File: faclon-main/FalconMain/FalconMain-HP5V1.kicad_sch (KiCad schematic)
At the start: 0 parts

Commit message: Reorganize
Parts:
- added C40, C53: 100uF, Capacitor_THT:CP_Radial_D8.0mm_P3.50mm, symbol Device:C_Polarized_Small
- added C41, C42, C43, C44: 10uF, Capacitor_SMD:C_1210_3225Metric, symbol Device:C_Small
- added C45, C47: 100nF, Capacitor_SMD:C_0402_1005Metric, symbol Device:C_Small
- added C46: 1uF, Capacitor_SMD:C_0603_1608Metric, symbol Device:C_Small
- added C48: 510pF, Capacitor_SMD:C_0402_1005Metric, symbol Device:C_Small
- added C49, C50, C51, C52: 47uF, Capacitor_SMD:C_1210_3225Metric, symbol Device:C_Small
- added C54: 51pF, Capacitor_SMD:C_0402_1005Metric, symbol Device:C_Small
- added C55: 1.5nF, Capacitor_SMD:C_0402_1005Metric, symbol Device:C_Small
- added L5: 2.0uH, JetkovKiCADLib:WE-HCI_1365_7443551, symbol Device:L_Small
- added Q22, Q23: Q_NMOS_LFPAK, JetkovKiCADLib:LFPACK56-S08_SOT669_NXP, symbol JetkovKiCADLib:Q_NMOS_LFPAK
- added R58, R59: 0R, Resistor_SMD:R_0402_1005Metric, symbol Device:R_Small
- added R60: DNP, Resistor_SMD:R_0402_1005Metric, symbol Device:R_Small
- added R61: 49.9k, Resistor_SMD:R_0402_1005Metric, symbol Device:R_Small
- added R62: 2R, Resistor_SMD:R_0402_1005Metric, symbol Device:R_Small
- added R63, R64: 80.6k, Resistor_SMD:R_0402_1005Metric, symbol Device:R_Small
- added R65: 27.4k, Resistor_SMD:R_0402_1005Metric, symbol Device:R_Small
- added R66: 100k, Resistor_SMD:R_0402_1005Metric, symbol Device:R_Small
- added R67: 15k, Resistor_SMD:R_0402_1005Metric, symbol Device:R_Small
- added U7: ADP1883ARMZ-0.6-R7, JetkovKiCADLib:10-MSOP_RM-10_AD, symbol JetkovKiCADLib:ADP1883ARMZ-0.6-R7
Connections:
- new net: R63.1, R67.2, U7.3 (FB)
- new net: C47.1, U7.10 (BST)
- new net: C48.1, C54.2, U7.2 (COMP/EN)
- new net: C45.2, C46.1, R59.1, U7.5 (VDD)
- new net: Q23.4 (G), R66.2, U7.6 (DRVL)
- new net: R58.2, U7.8 (DRVH)
- new net: C47.2, L5.1, Q22.1 (S), Q22.2 (S), Q22.3 (S), Q23.5 (D), R62.2, U7.9 (SW)
- new net: C48.2, R65.2
- new net: Q22.4 (G), R58.1
- new net: C55.1, R62.1
- new net +4V_SW: R59.2
- new net +5V1: C49.1, C50.1, C51.1, C52.1, C53.1, L5.2, R61.1, R63.2
- new net GND: C40.2, C41.1, C42.1, C43.1, C44.1, C45.1, C46.2, C49.2, C50.2, C51.2, C52.2, C53.2, C54.1, C55.2, Q23.1 (S), Q23.2 (S), Q23.3 (S), R64.1, R65.1, R66.1, R67.1, U7.4 (GND), U7.7 (PGND)
- new net VSENSE_5V1: R60.1, R61.2, R64.2
- new net VSYS_SW: C40.1, C41.2, C42.2, C43.2, C44.2, Q22.5 (D), R60.2, U7.1 (VIN)
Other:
- note added: "12-19.5V/4.7A to 5.1V/10A Buck Regulator"
- note added: "Accounting for DC bias: C_{OUT}=47*(1-0.424)*4=108uF"
- note added: "C@5.1V=27uF"
- note added: "Duty Cycle --------- D_{MIN}=5.1/19=0.268 D_{MAX}=5.1/12=0.425"
- note added: "HIGH POWER 5.1V REGULATION"
- note added: "Heatsink"
- note added: "Loop Compensation ---------------- f_{CROSS}=f_{SW}/12=600e3/12=50kHz f_{ZERO}=f_{CROSS}/4=12.5kHz R_{COMP}=[(f_{CROSS}/(F_{CROSS}+F_{ZERO})][2(pi)(f_{CROSS})(C_{OUT})/((G_{M})(A_{CS}))][V_{OUT}/V_{REF}] =[50e3/(50e3+12.5e3)][(2)(pi)(50e3)(C_{OUT})/((500e-6)(A_{CS})][V_{OUT}/0.8] =[(C_{OUT})(V_{OUT})/(A_{CS})][628318530.718] =[(108e-6)(5.1)/13.4][628318530.718] =25.83kOhms~=26.1kOhms -> 27.4kOhms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"
- note added: "MLCC @19V C=6uF"
- note added: "MOSFET Channel Conduction Loss --------------------- P_{N1,N2(CL)}=[D(R_{ON-UPPER})+(1-D)R_{ON-LOWER)}]I_{LOAD}^2 =[0.32(5e-3)+(1-0.32)(5e-3)]10^2 =0.16+0.34=0.5W MOSFET Driver Loss --------------------- V_{DR}=V_{DD}-V_{F(RECT)}=4-0.320=3.68V P_{DR(LOSS)}=V_{DR}[(f_{SW})(C_{G-UPPER})(V_{DR})+I_{BIAS}]+V_{DD}[(f_{SW})(C_{G-LOWER})(V_{DD})+I_{BIAS}] =3.68[(600e3)(2.5e-9)(3.68)+2e-3]+4[(600e3)(2.5e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"
- note added: "MOSFET PSMN4R1-30YLC -------------------- R_{DS(ON)@4V}=5mOhms V_{f(DIODE)@10A}=0.75V Q_{G(TOT)@4V}=10nC C_{G(TOT)@4V}=10nC/4V=2.5nF C_{iss}=1.5nF R_{G}=1.9Ohms"
- note added: "Make footprint compatible with ETQ-P5M2R0YLC"
- note added: "Maximum Inductor Ripple Current -------------------------------- dI_{L}=K_{I}(I_{LOAD}) ~=0.33(10)=3.3A Minimum Inductance -------------------------------- L=[(V_{IN}-V_{OUT})/((dI_{L})(f_{SW}))][V_{OUT}/V_{IN}] =[(16-5.1)/((3.3)(600e3))][5.1/16]=1.755uH Inductor Ripple Current with Selected Inductance -------------------------------- dI_{L}=[(16-5.1)/((2e-6)(600e3))][5.1/16]=2.895A K_{I}=2.895/1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"
- note added: "Minimum Input Capacitance -------------------- V_{CIN-MAX-RPL}=0.01(V_{IN-MIN})+([I_{LOAD-MAX})(ESR_{CIN}) =0.01(12)-(10)(0.005)=70mV C_{IN-MIN}=[I_{LOAD-MAX}/V_{MAX-RPL}][D(1-D)/f_{SW}] =[10/0.07][0.425(1-0.425)/600e3]=58.1uF Minimum Output Capacitance ------------------------- dV_{OUTRR}=(0.01)V_{OUT}=(0.005)5.1=0.051V C_{OUT}>dI_{L}/[(8)(f_{SW})(dV_{OUTRR}-(dI_{L})(ESR_{COUT}))] >2.895/[(8)(60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"
- note added: "Output Voltage Set ----------- R_{T}=R_{B}(V_{OUT}-0.8V)/0.8V =15e3(5.1-0.8)/0.8 =80.625k~=80.6k"
- note added: "P=CV^{2}(f_{SW}) =(1.5e-9)(5.1^2)(600e3)=0.023"
- note added: "Place as close to MOSFETs as possible"
- note added: "V_{DD}>=V_{IN}/8+1.5 =20/8+1.5=4V V_{DD}>=V_{OuT}/4 =5.1/4=1.275V"
- note added: "Valley Current Limiting -------------- I_{VC-LIM}=1.5V/((A_{CS})(R_{ON})) =1.5/((26.7)(5e-3)) =11.23 I_{LOAD-LIM}=I_{VC-LIM}/(1-K_{I}) =11.23/(1-0.29)=15.8A"

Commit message: Layout WIP
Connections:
- net 5V1_BCOMP: now reaches C48.1, C54.2, U7.2 (COMP/EN)
- net 5V1_BVDD: now reaches C45.2, C46.1, R59.1, U7.5 (VDD)
- net 5V1_BDRVL: now reaches Q23.4 (G), R66.2, U7.6 (DRVL)
- net 5V1_BSW: now reaches C47.2, L5.1, Q22.1 (S), Q22.2 (S), Q22.3 (S), Q23.5 (D), R62.2, U7.9 (SW)
- net 5V1_BDRVH: now reaches Q22.4 (G), R58.1
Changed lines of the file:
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@@
     (effects (font (size 1.27 1.27)) (justify left bottom))
+  )
+  (label "5V1_BSW" (at 123.19 64.77 0)
+    (effects (font (size 0.8 0.8)) (justify left bottom))
+  )
+  (label "5V1_BCOMP" (at 74.93 64.77 0)
+    (effects (font (size 0.8 0.8)) (justify left bottom))
+  )
+  (label "5V1_BDRVH" (at 118.11 54.61 0)
+    (effects (font (size 0.8 0.8)) (justify left bottom))
+  )
+  (label "5V1_BDRVL" (at 111.76 72.39 0)
+    (effects (font (size 0.8 0.8)) (justify left bottom))
+  )
+  (label "5V1_BVDD" (at 74.93 57.15 0)
+    (effects (font (size 0.8 0.8)) (justify left bottom))
   )
   (global_label "VSENSE_5V1" (shape output) (at 246.38 64.77 0) (fields_autoplaced)

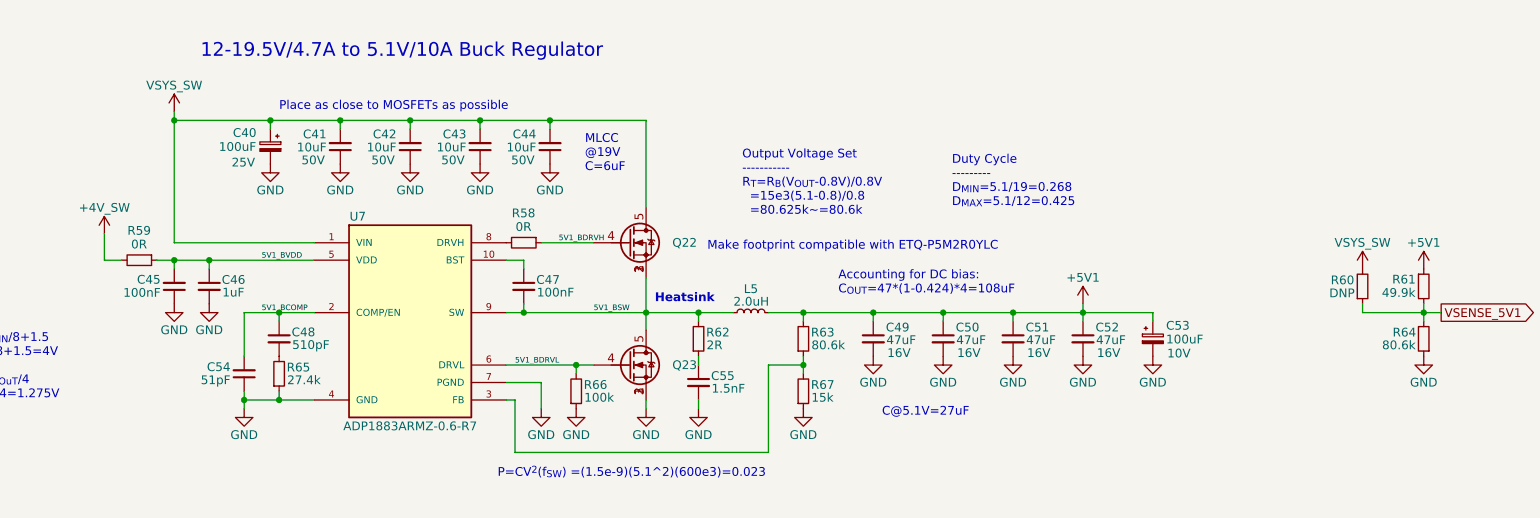
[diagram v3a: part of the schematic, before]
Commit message: Large component rough placement
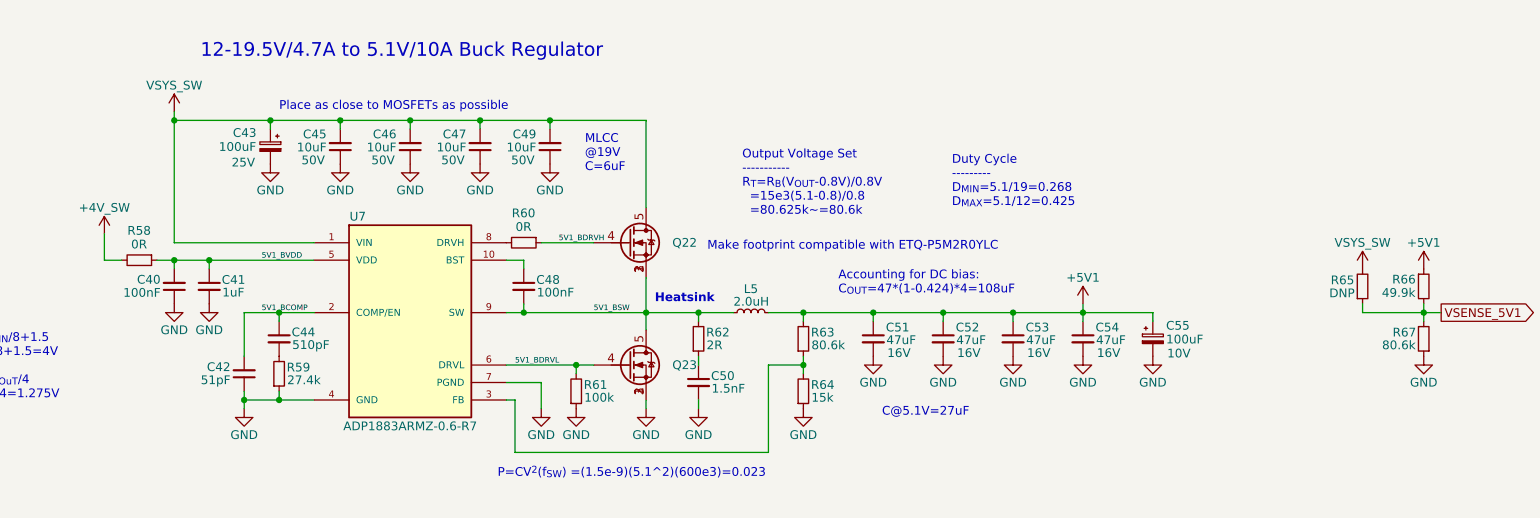
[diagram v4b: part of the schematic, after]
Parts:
- renumbered C45 to C40, C46 to C41, C54 to C42, C40 to C43, C48 to C44, C41 to C45, C42 to C46, C43 to C47, C47 to C48, C44 to C49, C55 to C50, C49 to C51, C50 to C52, C51 to C53, C52 to C54, C53 to C55, R59 to R58, R65 to R59, R58 to R60, R66 to R61, R67 to R64, R60 to R65, R61 to R66, R64 to R67

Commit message: Rought placement done
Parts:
- renumbered C40 to C42, C41 to C43, C42 to C44, C43 to C45, C44 to C46, C45 to C47, C46 to C48, C47 to C49, C48 to C50, C49 to C51, C50 to C52, C51 to C53, C52 to C54, C53 to C55, C54 to C56, C55 to C57
